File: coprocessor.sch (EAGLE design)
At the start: 1 part, among them IC1 ATMEGA32U2-TQFP

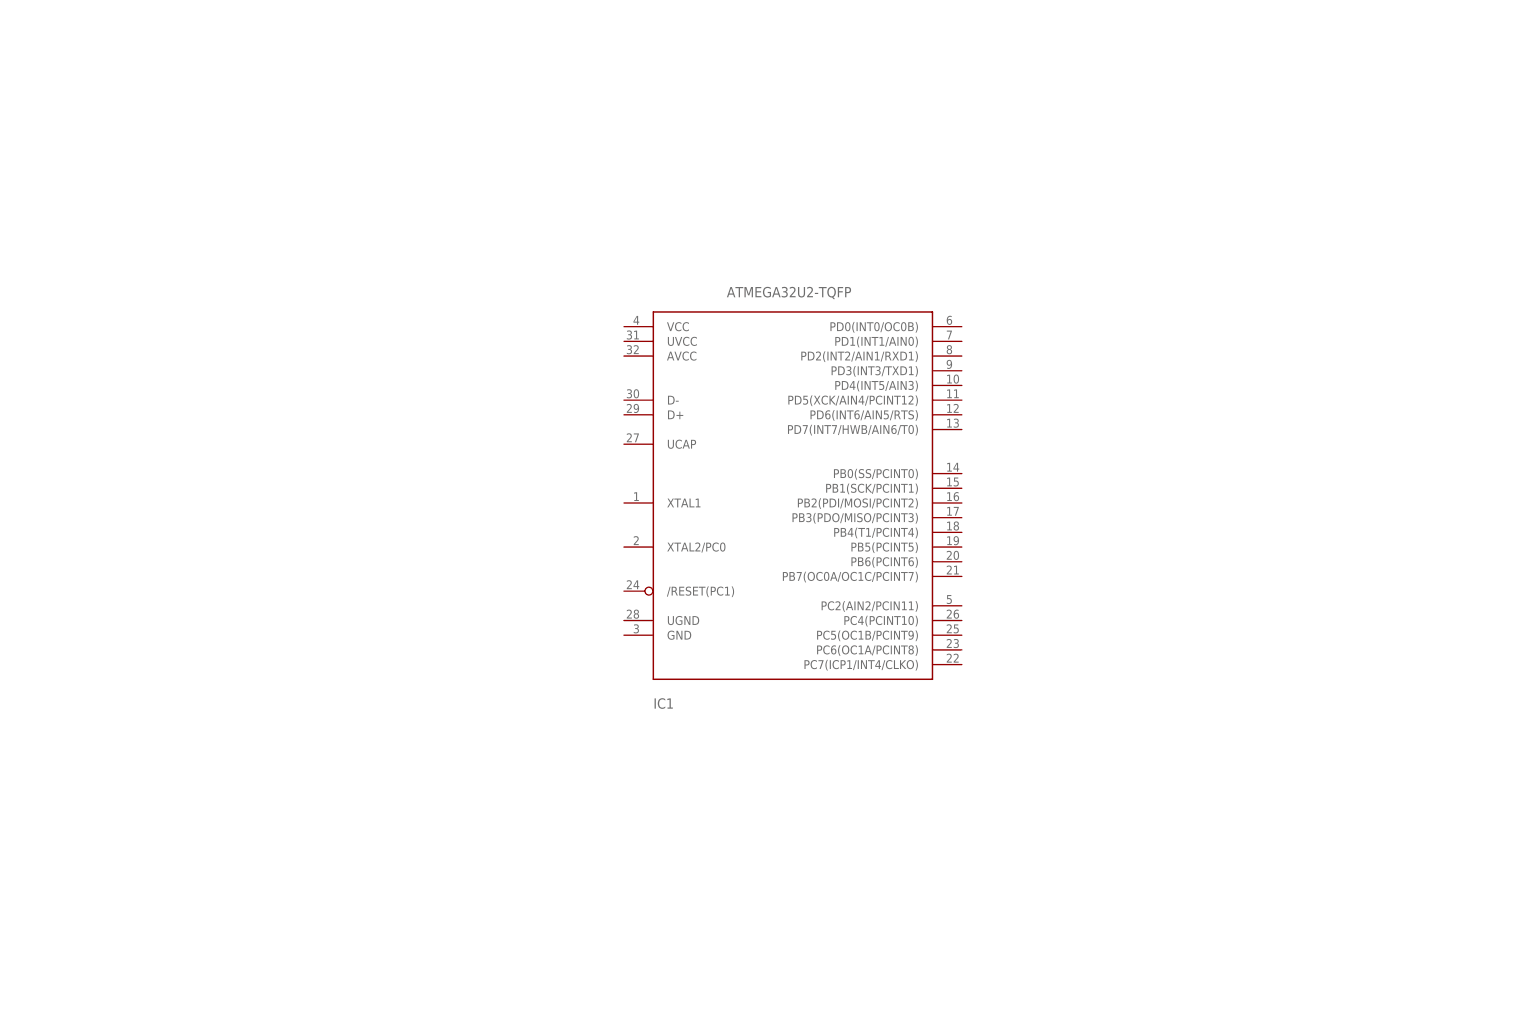
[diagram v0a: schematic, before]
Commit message: added the co-processor and whatnot
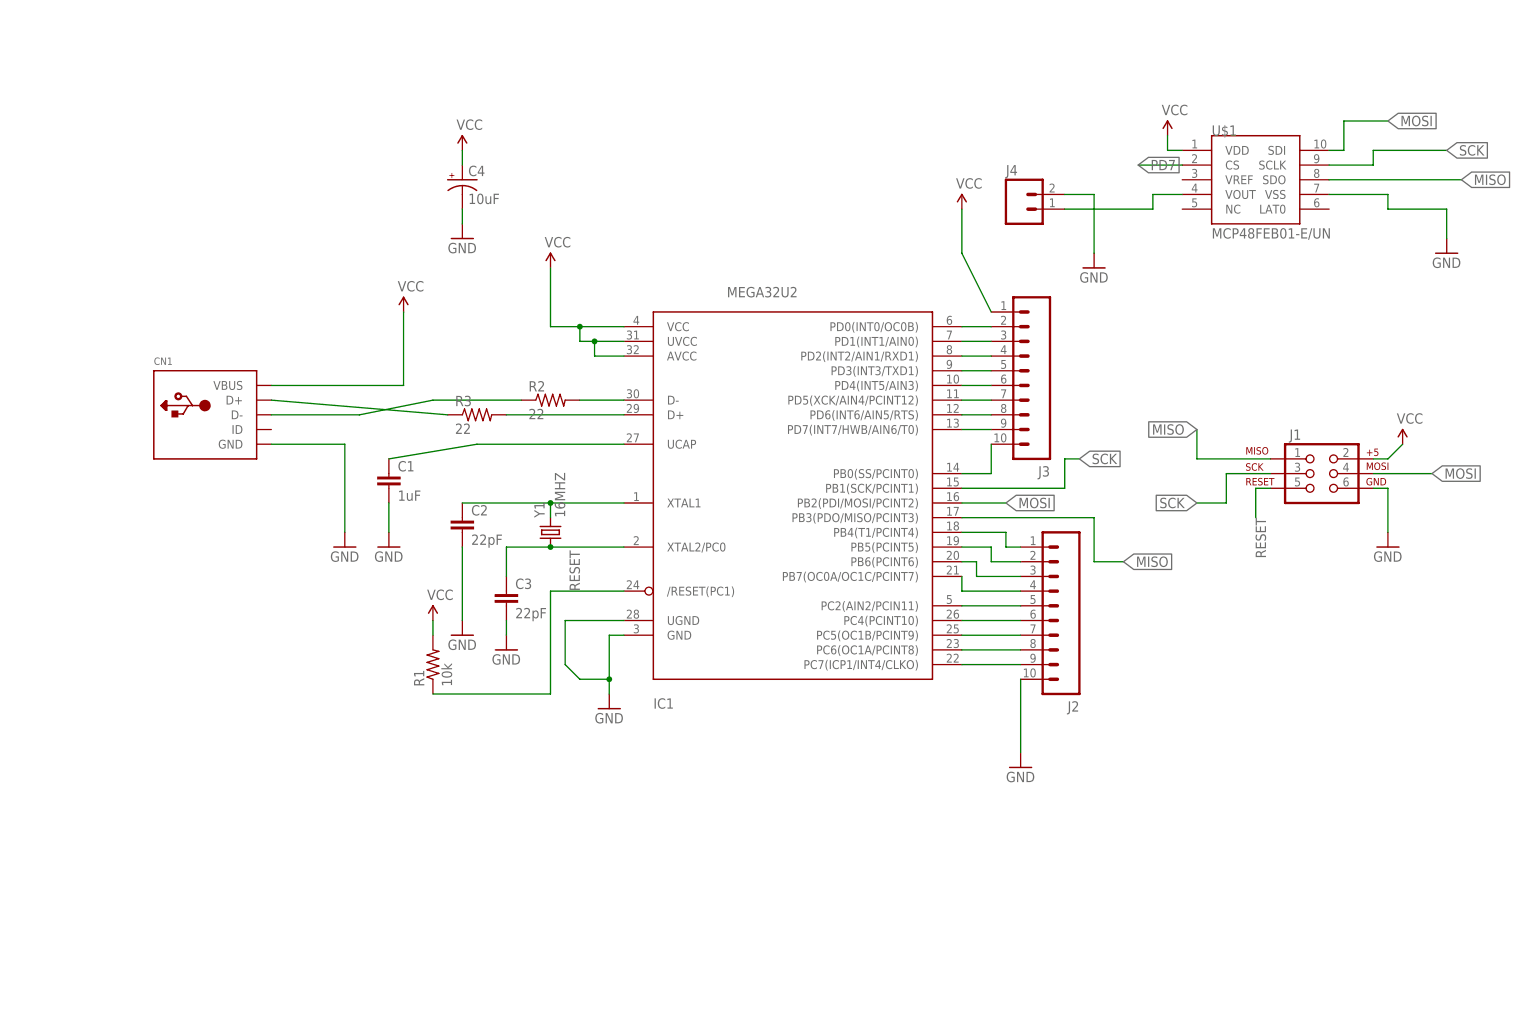
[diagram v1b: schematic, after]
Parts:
- added C1: 1uF, SparkFun-Capacitors:CAPPTH
- added C2, C3: 22pF, SparkFun-Capacitors:CAPPTH
- added C4: 10uF, SparkFun-Capacitors:CAP_POLPTH2
- added CN1: (no value), adafruit:USBTHM
- added J1: AVR_SPI_PRG_6NS, SparkFun-Connectors:AVR_SPI_PRG_6NS
- added J2, J3: (no value), SparkFun-Connectors:M10LOCK
- added J4: (no value), SparkFun-Connectors:M02POLAR
- added R1: 10k, SparkFun-Resistors:10KOHM-1/4W-1%(PTH)HORIZ-KIT
- added R2, R3: 22, SparkFun-Resistors:RESISTORPTH-1/4W
- added U$1: MCP48FEB01-E/UN, custom:MCP48FEB01-E/UN
- added Y1: 16MHZ, SparkFun-FreqCtrl:CRYSTALHC49UV
- IC1: value ATMEGA32U2-TQFP -> MEGA32U2
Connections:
- new net DAC_VOUT: J4.1, U$1.VOUT
- new net GND: C1.2, C2.2, C3.2, C4.-, CN1.GND, IC1.GND, IC1.UGND, J1.6, J2.10, J4.2, U$1.VSS
- new net MISO: IC1.PB3(PDO/MISO/PCINT3), J1.1, U$1.SDO
- new net MOSI: IC1.PB2(PDI/MOSI/PCINT2), J1.4, U$1.SDI
- new net N$10: C3.1, IC1.XTAL2/PC0, Y1.1
- new net N$4: IC1.D+, R3.2
- new net N$5: IC1.D-, R2.2
- new net N$6: CN1.D+, R3.1
- new net N$7: C1.1, IC1.UCAP
- new net N$8: CN1.D-, R2.1
- new net N$9: C2.1, IC1.XTAL1, Y1.2
- new net PB0: IC1.PB0(SS/PCINT0), J3.10
- new net PB4: IC1.PB4(T1/PCINT4), J2.1
- new net PB5: IC1.PB5(PCINT5), J2.2
- new net PB6: IC1.PB6(PCINT6), J2.3
- new net PB7: IC1.PB7(OC0A/OC1C/PCINT7), J2.4
- new net PC2: IC1.PC2(AIN2/PCIN11), J2.5
- new net PC4: IC1.PC4(PCINT10), J2.6
- new net PC5: IC1.PC5(OC1B/PCINT9), J2.7
- new net PC6: IC1.PC6(OC1A/PCINT8), J2.8
- new net PC7: IC1.PC7(ICP1/INT4/CLKO), J2.9
- new net PD0: IC1.PD0(INT0/OC0B), J3.2
- new net PD1: IC1.PD1(INT1/AIN0), J3.3
- new net PD2: IC1.PD2(INT2/AIN1/RXD1), J3.4
- new net PD3: IC1.PD3(INT3/TXD1), J3.5
- new net PD4: IC1.PD4(INT5/AIN3), J3.6
- new net PD5: IC1.PD5(XCK/AIN4/PCINT12), J3.7
- new net PD6: IC1.PD6(INT6/AIN5/RTS), J3.8
- new net PD7: IC1.PD7(INT7/HWB/AIN6/T0), J3.9, U$1.CS
- new net RESET: IC1./RESET(PC1), J1.5, R1.1
- new net SCK: IC1.PB1(SCK/PCINT1), J1.3, U$1.SCLK
- new net VCC: C4.+, CN1.VBUS, IC1.AVCC, IC1.UVCC, IC1.VCC, J1.2, J3.1, R1.2, U$1.VDD

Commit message: redid the routing by hand
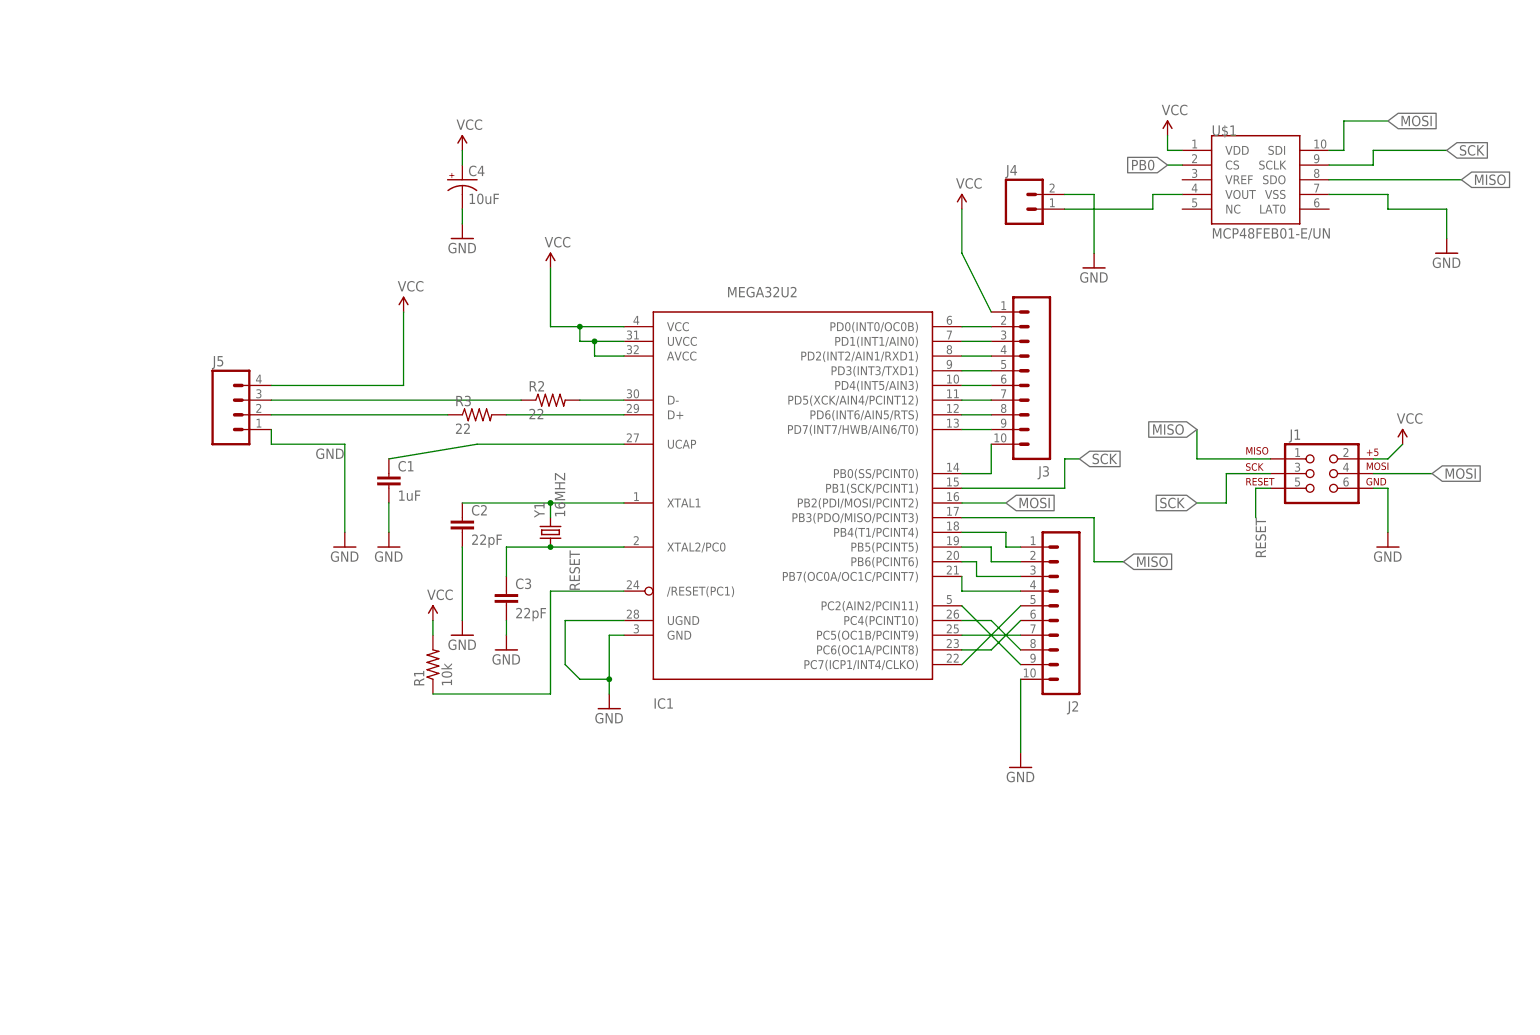
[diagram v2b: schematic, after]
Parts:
- removed CN1: (no value), adafruit:USBTHM
- added J5: (no value), SparkFun-Connectors:M04LOCK_LONGPADS
- J2, J3: device SparkFun-Connectors:M10LOCK -> SparkFun-Connectors:M102MM
- R1: device SparkFun-Resistors:10KOHM-1/4W-1%(PTH)HORIZ-KIT -> SparkFun-Resistors:RESISTOR0603-RES
- R2: device SparkFun-Resistors:RESISTORPTH-1/4W -> SparkFun-Resistors:RESISTOR0603-RES
- R3: device SparkFun-Resistors:RESISTORPTH-1/4W -> SparkFun-Resistors:RESISTOR0603
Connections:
- removed net N$6: CN1.D+, R3.1
- removed net N$8: CN1.D-, R2.1
- new net N$1: J5.2, R3.1
- new net N$4: J5.3, R2.1
- net GND: now also J5.1; no longer CN1.GND
- net PB0: now also U$1.CS
- net PC2: now also J2.9; no longer J2.5
- net PC4: now also J2.8; no longer J2.6
- net PC6: now also J2.6; no longer J2.8
- net PC7: now also J2.5; no longer J2.9
- net PD7: no longer U$1.CS
- net VCC: now also J5.4; no longer CN1.VBUS

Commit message: added the custom library and power controller
started to integrate the custom power controller to the coprocessor
board so it can be powered by the battery. I  need to figure out how to
enable the raspberry pi
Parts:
- removed J5: (no value), SparkFun-Connectors:M04LOCK_LONGPADS
- removed Y1: 16MHZ, SparkFun-FreqCtrl:CRYSTALHC49UV
- added C5: 0.1uF, SparkFun-Capacitors:0.1UF-100V-10%(0603)
- added C6: 1.0uF, SparkFun-Capacitors:1.0UF-16V-10%(0603)
- added C7: 2.2uF, SparkFun-Capacitors:2.2UF-10V-20%(0603)
- added C8: 10uF, SparkFun-Capacitors:10UF-6.3V-20%(0603)
- added CN1: (no value), adafruit:USBMINIB
- added FRAME2: FRAME-LETTERNO_PACKAGE, SparkFun-Aesthetics:FRAME-LETTERNO_PACKAGE
- added L1: 6.8uH, SparkFun-Coils:INDUCTOR-SDR13-27UH
- added R10, R12: 100k, SparkFun-Resistors:100KOHM-1/10W-1%(0603)
- added R11: 1K, SparkFun-Resistors:1KOHM-1/10W-1%(0603)
- added R4: 340, SparkFun-Resistors:340OHM-1/10W-1%(0603)
- added R5, R7: 1.86m, SparkFun-Resistors:1.8KOHM1/10W1%(0603)
- added R6, R8: 200k, SparkFun-Resistors:200KOHM1/10W1%(0603)200K
- added R9: 270k, SparkFun-Resistors:220KOHM1/10W1%(0603)
- added U$2: 16MHZ, custom:CRYSTAL-ABLS
- added U1: (no value), custom:TPS6103X
- added U2: (no value), custom:MCP73871
- C1, C2, C3: device SparkFun-Capacitors:CAPPTH -> SparkFun-Capacitors:CAP0805
- C4: device SparkFun-Capacitors:CAP_POLPTH2 -> SparkFun-Capacitors:CAP_POLSMD
- R1, R2: device SparkFun-Resistors:RESISTOR0603-RES -> SparkFun-Resistors:RESISTOR0805-RES
- R3: device SparkFun-Resistors:RESISTOR0603 -> SparkFun-Resistors:RESISTOR0805-RES
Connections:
- new net 5V: C7.1, R7.2, U1.VOUT
- new net DATA+: CN1.D+, R2.1
- new net DATA-: CN1.D-, R3.1
- new net N$11: L1.2, U1.SW
- new net N$12: R11.2, U2.PROG1
- new net N$13: R7.1, R8.2, U1.FB
- new net N$14: R12.2, U2.PROG3
- new net N$6: R4.2, R5.1, U1.LBI
- new net V_BATT: C5.1, C6.1, L1.1, R5.2, R6.2, U1.VBAT, U2.VOUT1, U2.VOUT2
- new net V_USB: C8.1, CN1.VBUS, R9.2, U2./TE, U2.CE, U2.PROG2, U2.SEL, U2.VIN1, U2.VIN2
- net GND: now also C5.2, C6.2, C7.2, C8.2, CN1.GND, R10.1, R11.1, R12.1, R4.1, R8.1, U1.GND, U1.PGND, U1.SYNC, U2.THERMAL, U2.VSS1, U2.VSS2; no longer J5.1
- net N$1: now also R10.2, R9.1, U2.VPCC; no longer J5.2, R3.1
- net N$10: now also U$2.P$1; no longer Y1.1
- net N$4: now also R6.1, U1.EN; no longer J5.3, R2.1
- net N$9: now also U$2.P$2; no longer Y1.2
- net VCC: no longer J5.4

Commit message: finished the power
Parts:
- added B1: (no value), custom:MICROBUILDER_BATTERY
- added C10: (no value), SparkFun-Capacitors:CAP_POL1206
- added C9: 10uF, SparkFun-Capacitors:10UF-6.3V-20%(0603)
- added D2: (no value), custom:MICROBUILDER_LED0603
- added LOGO1: OSHW-LOGOS, SparkFun-Aesthetics:OSHW-LOGOS
- added R13: 1K, SparkFun-Resistors:1KOHM-1/10W-1%(0603)
- added T1: (no value), custom:TRANSISTOR_PNP_DRIVERMUN2111T1SC59-BEC
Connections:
- new net N$15: T1.B, U1.LBO
- new net N$16: R13.2, T1.C
- new net N$17: D2.A, R13.1
- new net N$8: B1.+, C9.1, U2.VBAT1, U2.VBAT2, U2.VBATSENS
- net 5V: now also C10.+
- net GND: now also B1.-, C10.-, C9.2, D2.C
- net V_BATT: now also T1.E
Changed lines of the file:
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@@
 <part name="GND21" library="SparkFun-Aesthetics" deviceset="GND" device=""/>
 <part name="SUPPLY14" library="SparkFun-Aesthetics" deviceset="V_BATT" device=""/>
+<part name="B1" library="custom" deviceset="MICROBUILDER_BATTERY" device=""/>
+<part name="LOGO1" library="SparkFun-Aesthetics" deviceset="OSHW-LOGO" device="S"/>
+<part name="C9" library="SparkFun-Capacitors" deviceset="10UF-6.3V-20%(0603)" device="" value="10uF"/>
+<part name="GND22" library="SparkFun-Aesthetics" deviceset="GND" device=""/>
+<part name="GND23" library="SparkFun-Aesthetics" deviceset="GND" device=""/>
+<part name="T1" library="custom" deviceset="TRANSISTOR_PNP_DRIVER" device="SC59-BEC" technology="MUN2111T1"/>
+<part name="SUPPLY15" library="SparkFun-Aesthetics" deviceset="V_BATT" device=""/>
+<part name="R13" library="SparkFun-Resistors" deviceset="1KOHM-1/10W-1%(0603)" device="" value="1K"/>
+<part name="D2" library="custom" deviceset="MICROBUILDER_LED" device="0603"/>
+<part name="GND24" library="SparkFun-Aesthetics" deviceset="GND" device=""/>
+<part name="C10" library="SparkFun-Capacitors" deviceset="CAP_POL" device="1206"/>
+<part name="GND25" library="SparkFun-Aesthetics" deviceset="GND" device=""/>
 </parts>
 <sheets>
@@
 <instance part="GND21" gate="1" x="256.54" y="137.16"/>
 <instance part="SUPPLY14" gate="G$1" x="259.08" y="177.8"/>
+<instance part="B1" gate="G$1" x="276.86" y="160.02" rot="R90"/>
+<instance part="LOGO1" gate="G$1" x="266.7" y="93.98"/>
+<instance part="C9" gate="G$1" x="264.16" y="160.02"/>
+<instance part="GND22" gate="1" x="264.16" y="149.86"/>
+<instance part="GND23" gate="1" x="276.86" y="149.86"/>
+<instance part="T1" gate="G$1" x="172.72" y="45.72"/>
+<instance part="SUPPLY15" gate="G$1" x="175.26" y="50.8"/>
+<instance part="R13" gate="G$1" x="175.26" y="35.56" rot="R90"/>
+<instance part="D2" gate="G$1" x="175.26" y="25.4" rot="R270"/>
+<instance part="GND24" gate="1" x="175.26" y="20.32"/>
+<instance part="C10" gate="G$1" x="182.88" y="81.28"/>
+<instance part="GND25" gate="1" x="182.88" y="73.66"/>
 </instances>
 <busses>
@@
 <wire x1="254" y1="147.32" x2="254" y2="144.78" width="0.1524" layer="91"/>
 <junction x="254" y="144.78"/>
+</segment>
+<segment>
+<pinref part="C9" gate="G$1" pin="2"/>
+<pinref part="GND22" gate="1" pin="GND"/>
+<wire x1="264.16" y1="157.48" x2="264.16" y2="152.4" width="0.1524" layer="91"/>
+</segment>
+<segment>
+<pinref part="B1" gate="G$1" pin="-"/>
+<pinref part="GND23" gate="1" pin="GND"/>
+<wire x1="276.86" y1="157.48" x2="276.86" y2="152.4" width="0.1524" layer="91"/>
+</segment>
+<segment>
+<pinref part="D2" gate="G$1" pin="C"/>
+<pinref part="GND24" gate="1" pin="GND"/>
+</segment>
+<segment>
+<pinref part="C10" gate="G$1" pin="-"/>
+<pinref part="GND25" gate="1" pin="GND"/>
 </segment>
 </net>
@@
 <junction x="256.54" y="177.8"/>
 </segment>
+<segment>
+<pinref part="T1" gate="G$1" pin="E"/>
+<pinref part="SUPPLY15" gate="G$1" pin="V_BATT"/>
+</segment>
 </net>
 <net name="N$11" class="0">
@@
 <pinref part="SUPPLY10" gate="G$1" pin="5V"/>
 <wire x1="162.56" y1="86.36" x2="170.18" y2="86.36" width="0.1524" layer="91"/>
-<wire x1="170.18" y1="86.36" x2="185.42" y2="86.36" width="0.1524" layer="91"/>
+<wire x1="170.18" y1="86.36" x2="182.88" y2="86.36" width="0.1524" layer="91"/>
+<wire x1="182.88" y1="86.36" x2="185.42" y2="86.36" width="0.1524" layer="91"/>
 <wire x1="185.42" y1="86.36" x2="185.42" y2="91.44" width="0.1524" layer="91"/>
 <pinref part="R7" gate="G$1" pin="2"/>
@@
 <wire x1="154.94" y1="86.36" x2="162.56" y2="86.36" width="0.1524" layer="91"/>
 <junction x="162.56" y="86.36"/>
+<pinref part="C10" gate="G$1" pin="+"/>
+<wire x1="182.88" y1="83.82" x2="182.88" y2="86.36" width="0.1524" layer="91"/>
+<junction x="182.88" y="86.36"/>
 </segment>
 </net>
@@
 </segment>
 </net>
+<net name="N$8" class="0">
+<segment>
+<pinref part="U2" gate="G$1" pin="VBAT1"/>
+<pinref part="B1" gate="G$1" pin="+"/>
+<wire x1="251.46" y1="167.64" x2="256.54" y2="167.64" width="0.1524" layer="91"/>
+<wire x1="256.54" y1="167.64" x2="264.16" y2="167.64" width="0.1524" layer="91"/>
+<wire x1="264.16" y1="167.64" x2="276.86" y2="167.64" width="0.1524" layer="91"/>
+<wire x1="276.86" y1="167.64" x2="276.86" y2="162.56" width="0.1524" layer="91"/>
+<pinref part="C9" gate="G$1" pin="1"/>
+<wire x1="264.16" y1="165.1" x2="264.16" y2="167.64" width="0.1524" layer="91"/>
+<junction x="264.16" y="167.64"/>
+<pinref part="U2" gate="G$1" pin="VBAT2"/>
+<wire x1="251.46" y1="165.1" x2="254" y2="165.1" width="0.1524" layer="91"/>
+<wire x1="254" y1="165.1" x2="256.54" y2="165.1" width="0.1524" layer="91"/>
+<wire x1="256.54" y1="165.1" x2="256.54" y2="167.64" width="0.1524" layer="91"/>
+<junction x="256.54" y="167.64"/>
+<pinref part="U2" gate="G$1" pin="VBATSENS"/>
+<wire x1="251.46" y1="162.56" x2="254" y2="162.56" width="0.1524" layer="91"/>
+<wire x1="254" y1="162.56" x2="254" y2="165.1" width="0.1524" layer="91"/>
+<junction x="254" y="165.1"/>
+</segment>
+</net>
+<net name="N$15" class="0">
+<segment>
+<pinref part="U1" gate="G$1" pin="LBO"/>
+<wire x1="139.7" y1="66.04" x2="147.32" y2="66.04" width="0.1524" layer="91"/>
+<wire x1="147.32" y1="66.04" x2="147.32" y2="45.72" width="0.1524" layer="91"/>
+<wire x1="147.32" y1="45.72" x2="165.1" y2="45.72" width="0.1524" layer="91"/>
+<pinref part="T1" gate="G$1" pin="B"/>
+</segment>
+</net>
+<net name="N$16" class="0">
+<segment>
+<pinref part="T1" gate="G$1" pin="C"/>
+<pinref part="R13" gate="G$1" pin="2"/>
+</segment>
+</net>
+<net name="N$17" class="0">
+<segment>
+<pinref part="R13" gate="G$1" pin="1"/>
+<pinref part="D2" gate="G$1" pin="A"/>
+</segment>
+</net>
